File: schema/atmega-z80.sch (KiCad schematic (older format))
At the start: 66 parts, among them J1 USB Connector, J2 Programmer ISP 10, J3 SPI Connector, J4 I2C Connector, Q1 PNP_2N4403, Q2 PNP_2N4403, Q3 NPN_2N4401, Q4 PNP_2N4403, U1 Z84C0010PEG, U2 ATmega324A-PU, U3 AS6C4008-55PCN, U4 SN74HC373N, U5 SN74HC257, U6 SN74HC257, U7 SN74HC00, U8 MCP2221AxP, Y1 20MHz

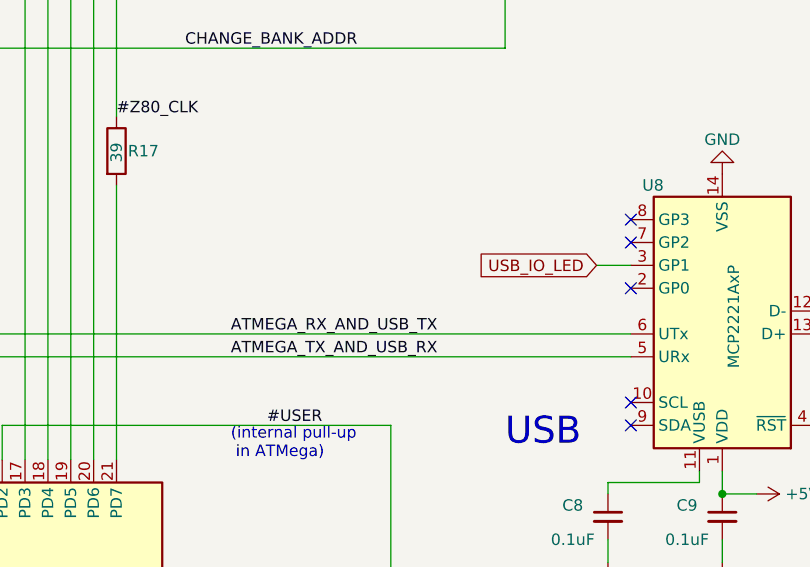
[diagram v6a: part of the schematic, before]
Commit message: improving USB IO LED
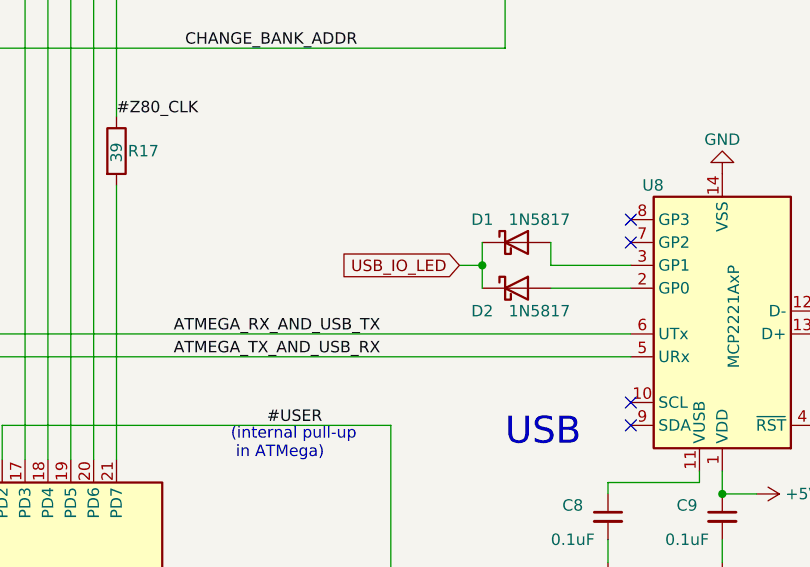
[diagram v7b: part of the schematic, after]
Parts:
- added D1, D2: 1N5817, Diode_THT:D_DO-41_SOD81_P10.16mm_Horizontal, symbol Diode:1N5817
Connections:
- net USB_IO_LED: now also D1.1 (K), D2.1 (K); no longer U8.3 (GP1)
- net at U8.2 (GP0): now also D2.2 (A)
- new net: D1.2 (A), U8.3 (GP1)
- no-connect marks 13 -> 12
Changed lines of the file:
@@
 Sheet 1 1
 Title "ATMega-Z80"
-Date "2021-09-12"
-Rev "V0.3"
+Date "2021-09-13"
+Rev "V0.4"
 Comp "https://github.com/symat/atmega-z80"
 Comment1 "Open project, licensed under BSD-3."
@@
 	-1   0    0    1
 $EndComp
-Wire Wire Line
-	9050 8000 9200 8000
-Text GLabel 9050 8000 0    50   Input ~ 0
+Text GLabel 8450 8000 0    50   Input ~ 0
 USB_IO_LED
 NoConn ~ 9200 7800
 NoConn ~ 9200 7900
-NoConn ~ 9200 8100
 NoConn ~ 9200 8600
 NoConn ~ 9200 8700
@@
 	-1   0    0    1
 $EndComp
-Text Label 7450 8300 0    50   ~ 0
+Text Label 7200 8300 0    50   ~ 0
 ATMEGA_RX_AND_USB_TX
-Text Label 7450 8400 0    50   ~ 0
+Text Label 7200 8400 0    50   ~ 0
 ATMEGA_TX_AND_USB_RX
 Wire Wire Line
@@
 Wire Notes Line
 	10650 6850 13400 6850
+$Comp
+L Diode:1N5817 D2
+U 1 1 61418E5F
+P 8700 8100
+F 0 "D2" H 8550 8000 50  0000 C CNN
+F 1 "1N5817" H 8800 8000 50  0000 C CNN
+F 2 "Diode_THT:D_DO-41_SOD81_P10.16mm_Horizontal" H 8700 7925 50  0001 C CNN
+F 3 "http://www.vishay.com/docs/88525/1n5817.pdf" H 8700 8100 50  0001 C CNN
+	1    8700 8100
+	1    0    0    -1
+$EndComp
+$Comp
+L Diode:1N5817 D1
+U 1 1 6141BB94
+P 8700 7900
+F 0 "D1" H 8550 8000 50  0000 C CNN
+F 1 "1N5817" H 8800 8000 50  0000 C CNN
+F 2 "Diode_THT:D_DO-41_SOD81_P10.16mm_Horizontal" H 8700 7725 50  0001 C CNN
+F 3 "http://www.vishay.com/docs/88525/1n5817.pdf" H 8700 7900 50  0001 C CNN
+	1    8700 7900
+	1    0    0    -1
+$EndComp
+Wire Wire Line
+	9200 8100 8850 8100
+Wire Wire Line
+	9200 8000 8850 8000
+Wire Wire Line
+	8850 8000 8850 7900
+Wire Wire Line
+	8550 7900 8550 8000
+Wire Wire Line
+	8450 8000 8550 8000
 Wire Bus Line
 	8550 2100 8550 3250
@@
 Wire Bus Line
 	5250 2100 5250 5600
+Connection ~ 8550 8000
+Wire Wire Line
+	8550 8000 8550 8100
 $EndSCHEMATC

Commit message: Preliminary PCB layout
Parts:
- D1, D2, D3, D4, D5, D6, D7: footprint LED_THT:LED_D3.0mm -> LED_THT:LED_D5.0mm
- J3: footprint (none) -> Connector_PinHeader_2.54mm:PinHeader_1x06_P2.54mm_Vertical
- J4: footprint (none) -> Connector_PinHeader_2.54mm:PinHeader_1x04_P2.54mm_Vertical
- renumbered D1 to D8, D2 to D9, SW_RESET to SW_RESET1, SW_USER to SW_USER1
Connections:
- net #SPI_SS: now also J3.2 (Pin_2); no longer J3.3 (Pin_3)
- net SPI_MISO: now also J3.4 (Pin_4); no longer J3.5 (Pin_5)
- net SPI_MOSI: now also J3.3 (Pin_3); no longer J3.2 (Pin_2)
- net SPI_SCK: now also J3.5 (Pin_5); no longer J3.4 (Pin_4)
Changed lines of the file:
@@
 	3150 9450 3150 9550
 $Comp
-L Switch:SW_Push SW_USER
+L Switch:SW_Push SW_USER1
 U 1 1 62362542
 P 8900 10850
-F 0 "SW_USER" H 8900 11043 50  0000 C CNN
+F 0 "SW_USER1" H 8900 11043 50  0000 C CNN
 F 1 "SW_Push" H 8900 11044 50  0001 C CNN
 F 2 "Button_Switch_THT:SW_PUSH_6mm_H5mm" H 8900 11050 50  0001 C CNN
@@
 	3750 10900 3750 10950
 $Comp
-L Switch:SW_Push SW_RESET
+L Switch:SW_Push SW_RESET1
 U 1 1 625E0418
 P 7150 10850
-F 0 "SW_RESET" H 7150 11043 50  0000 C CNN
+F 0 "SW_RESET1" H 7150 11043 50  0000 C CNN
 F 1 "SW_Push" H 7150 11044 50  0001 C CNN
 F 2 "Button_Switch_THT:SW_PUSH_6mm_H5mm" H 7150 11050 50  0001 C CNN
@@
 F 0 "D6" H 15050 8050 50  0000 C CNN
 F 1 "LED_Z80_ACTIVE" H 14850 7800 50  0000 C CNN
-F 2 "LED_THT:LED_D3.0mm" H 14950 7950 50  0001 C CNN
+F 2 "LED_THT:LED_D5.0mm" H 14950 7950 50  0001 C CNN
 F 3 "~" H 14950 7950 50  0001 C CNN
 	1    14950 7950
@@
 F 0 "D5" H 15250 7550 50  0000 C CNN
 F 1 "LED_PWR" H 15100 7300 50  0000 C CNN
-F 2 "LED_THT:LED_D3.0mm" H 15150 7450 50  0001 C CNN
+F 2 "LED_THT:LED_D5.0mm" H 15150 7450 50  0001 C CNN
 F 3 "~" H 15150 7450 50  0001 C CNN
 	1    15150 7450
@@
 F 0 "D1" H 15100 4650 50  0000 C CNN
 F 1 "LED_USB_IO" H 14950 4400 50  0000 C CNN
-F 2 "LED_THT:LED_D3.0mm" H 15000 4550 50  0001 C CNN
+F 2 "LED_THT:LED_D5.0mm" H 15000 4550 50  0001 C CNN
 F 3 "~" H 15000 4550 50  0001 C CNN
 	1    15000 4550
@@
 F 0 "D2" H 15100 5150 50  0000 C CNN
 F 1 "LED_CPU_IO" H 14950 4900 50  0000 C CNN
-F 2 "LED_THT:LED_D3.0mm" H 15000 5050 50  0001 C CNN
+F 2 "LED_THT:LED_D5.0mm" H 15000 5050 50  0001 C CNN
 F 3 "~" H 15000 5050 50  0001 C CNN
 	1    15000 5050
@@
 F 0 "D3" H 14650 5650 50  0000 C CNN
 F 1 "LED_EXT_MEM" H 14500 5400 50  0000 C CNN
-F 2 "LED_THT:LED_D3.0mm" H 14550 5550 50  0001 C CNN
+F 2 "LED_THT:LED_D5.0mm" H 14550 5550 50  0001 C CNN
 F 3 "~" H 14550 5550 50  0001 C CNN
 	1    14550 5550
@@
 F 0 "D7" H 14650 9350 50  0000 C CNN
 F 1 "LED_USER" H 14500 9100 50  0000 C CNN
-F 2 "LED_THT:LED_D3.0mm" H 14550 9250 50  0001 C CNN
+F 2 "LED_THT:LED_D5.0mm" H 14550 9250 50  0001 C CNN
 F 3 "~" H 14550 9250 50  0001 C CNN
 	1    14550 9250
@@
 F 0 "D4" H 14650 6450 50  0000 C CNN
 F 1 "LED_MEM" H 14500 6200 50  0000 C CNN
-F 2 "LED_THT:LED_D3.0mm" H 14550 6350 50  0001 C CNN
+F 2 "LED_THT:LED_D5.0mm" H 14550 6350 50  0001 C CNN
 F 3 "~" H 14550 6350 50  0001 C CNN
 	1    14550 6350
@@
 	12450 7200 12800 7200
 $Comp
-L power:+5V #PWR?
+L power:+5V #PWR0154
 U 1 1 62FDA9D8
 P 12800 7100
-F 0 "#PWR?" H 12800 6950 50  0001 C CNN
+F 0 "#PWR0154" H 12800 6950 50  0001 C CNN
 F 1 "+5V" V 12800 7300 50  0000 C CNN
 F 2 "" H 12800 7100 50  0001 C CNN
@@
 $EndComp
 $Comp
-L power:GND #PWR?
+L power:GND #PWR0155
 U 1 1 62FFE41E
 P 12800 7400
-F 0 "#PWR?" H 12800 7150 50  0001 C CNN
+F 0 "#PWR0155" H 12800 7150 50  0001 C CNN
 F 1 "GND" V 12800 7200 50  0000 C CNN
 F 2 "" H 12800 7400 50  0001 C CNN
@@
 F 0 "J4" H 12950 7400 50  0000 L CNN
 F 1 "I2C Connector" H 12750 6850 50  0000 L CNN
-F 2 "" H 13000 7200 50  0001 C CNN
+F 2 "Connector_PinHeader_2.54mm:PinHeader_1x04_P2.54mm_Vertical" H 13000 7200 50  0001 C CNN
 F 3 "~" H 13000 7200 50  0001 C CNN
 	1    13000 7200
@@
 F 0 "J3" H 11700 7600 50  0000 L CNN
 F 1 "SPI Connector" H 11500 6850 50  0000 L CNN
-F 2 "" H 11750 7300 50  0001 C CNN
+F 2 "Connector_PinHeader_2.54mm:PinHeader_1x06_P2.54mm_Vertical" H 11750 7300 50  0001 C CNN
 F 3 "~" H 11750 7300 50  0001 C CNN
 	1    11750 7300
 	1    0    0    -1
 $EndComp
+Text GLabel 11200 7400 0    50   Input ~ 0
+SPI_MISO
+Text GLabel 11200 7200 0    50   Input ~ 0
+#SPI_SS
+Text GLabel 11200 7300 0    50   Input ~ 0
+SPI_MOSI
 Text GLabel 11200 7500 0    50   Input ~ 0
-SPI_MISO
-Text GLabel 11200 7300 0    50   Input ~ 0
-#SPI_SS
-Text GLabel 11200 7200 0    50   Input ~ 0
-SPI_MOSI
-Text GLabel 11200 7400 0    50   Input ~ 0
 SPI_SCK
 $Comp
-L power:GND #PWR?
+L power:GND #PWR0156
 U 1 1 6321E910
 P 11550 7600
-F 0 "#PWR?" H 11550 7350 50  0001 C CNN
+F 0 "#PWR0156" H 11550 7350 50  0001 C CNN
 F 1 "GND" V 11550 7400 50  0000 C CNN
 F 2 "" H 11550 7600 50  0001 C CNN
@@
 $EndComp
 $Comp
-L power:+5V #PWR?
+L power:+5V #PWR0157
 U 1 1 63265105
 P 11550 7100
-F 0 "#PWR?" H 11550 6950 50  0001 C CNN
+F 0 "#PWR0157" H 11550 6950 50  0001 C CNN
 F 1 "+5V" V 11550 7300 50  0000 C CNN
 F 2 "" H 11550 7100 50  0001 C CNN
@@
 	10650 6850 13400 6850
 $Comp
-L Diode:1N5817 D2
+L Diode:1N5817 D9
 U 1 1 61418E5F
 P 8700 8100
-F 0 "D2" H 8550 8000 50  0000 C CNN
+F 0 "D9" H 8550 8000 50  0000 C CNN
 F 1 "1N5817" H 8800 8000 50  0000 C CNN
 F 2 "Diode_THT:D_DO-41_SOD81_P10.16mm_Horizontal" H 8700 7925 50  0001 C CNN
@@
 $EndComp
 $Comp
-L Diode:1N5817 D1
+L Diode:1N5817 D8
 U 1 1 6141BB94
 P 8700 7900
-F 0 "D1" H 8550 8000 50  0000 C CNN
+F 0 "D8" H 8550 8000 50  0000 C CNN
 F 1 "1N5817" H 8800 8000 50  0000 C CNN
 F 2 "Diode_THT:D_DO-41_SOD81_P10.16mm_Horizontal" H 8700 7725 50  0001 C CNN
@@
 Wire Wire Line
 	8450 8000 8550 8000
+Connection ~ 8550 8000
+Wire Wire Line
+	8550 8000 8550 8100
 Wire Bus Line
 	8550 2100 8550 3250
@@
 Wire Bus Line
 	5250 2100 5250 5600
-Connection ~ 8550 8000
-Wire Wire Line
-	8550 8000 8550 8100
 $EndSCHEMATC
